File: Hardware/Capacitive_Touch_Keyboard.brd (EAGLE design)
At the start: 170.2 x 68.6 mm, 47 parts, among them J1 AVR_SPI_PRG_6PTH, U2 MC34063DIP, U3 ATMEGA328P_PDIP_EZ, Y1 16MHz

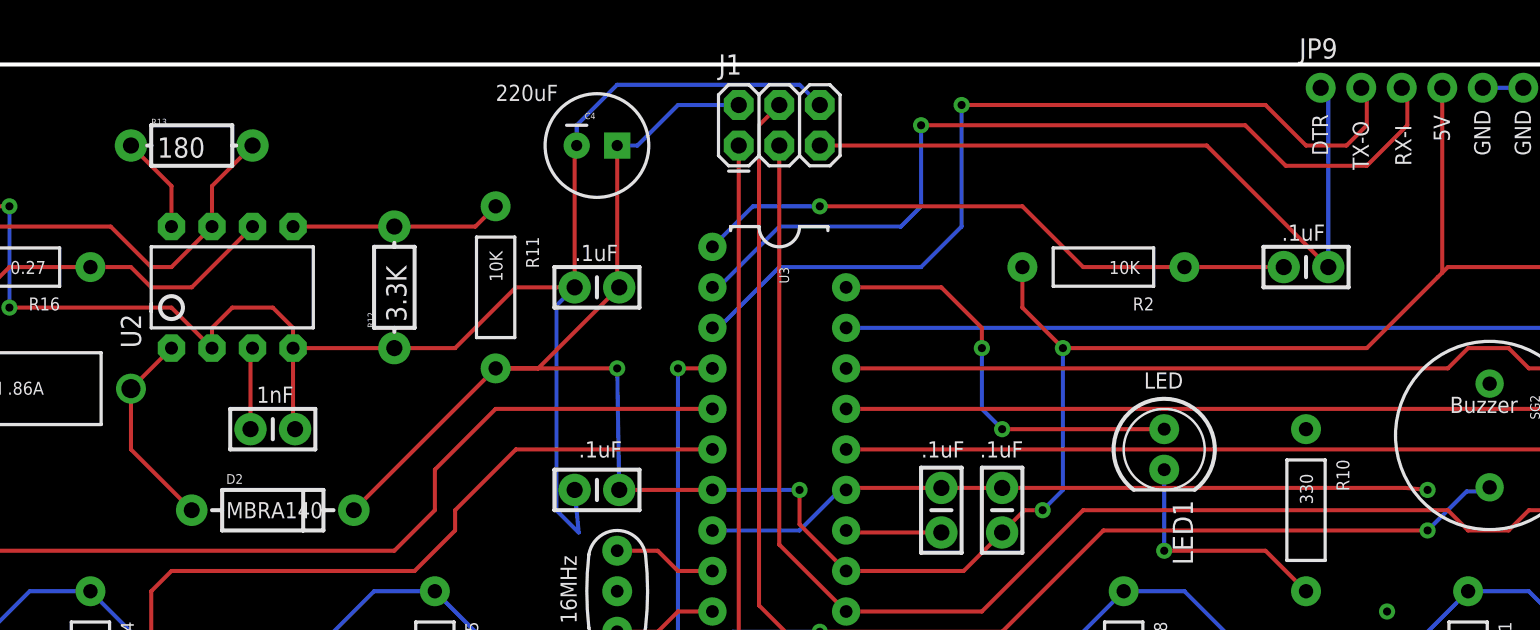
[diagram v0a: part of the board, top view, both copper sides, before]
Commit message: Updated resistor packages for v03
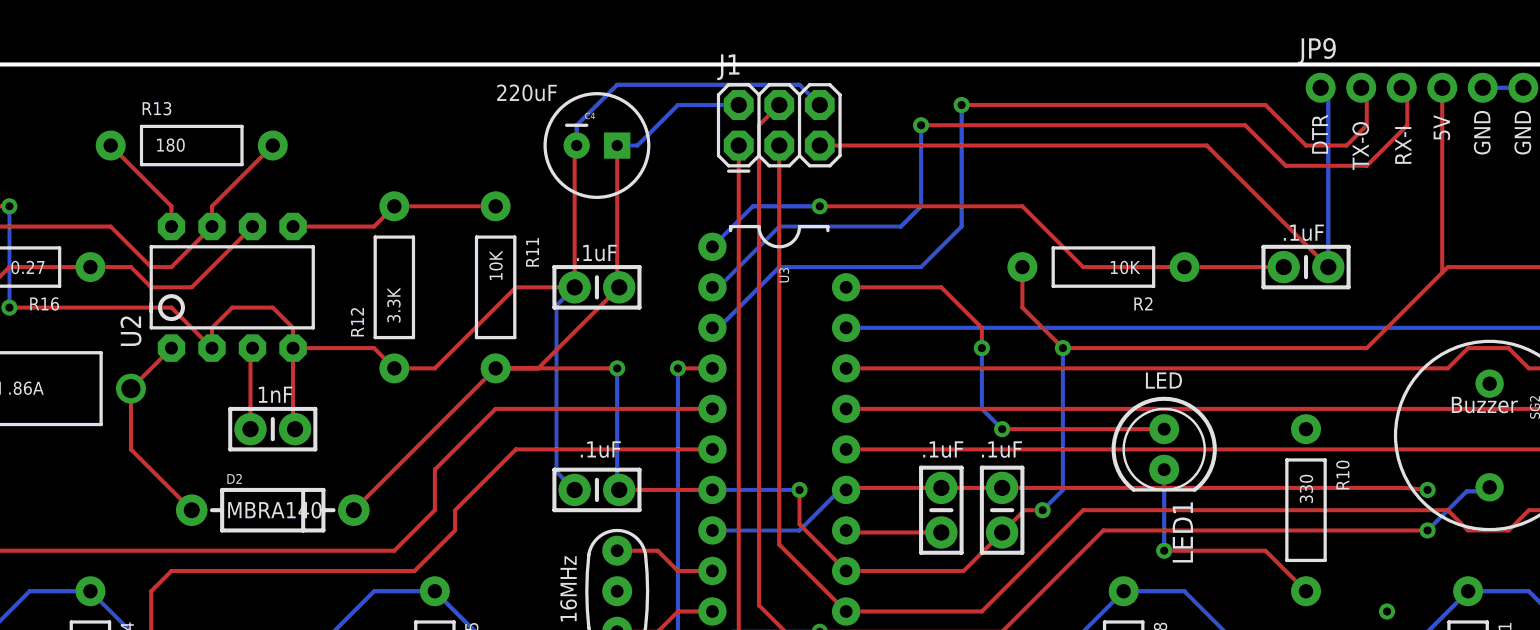
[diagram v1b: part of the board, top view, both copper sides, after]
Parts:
- R12, R13: device SparkFun-Resistors:AXIAL-0.3-KIT -> SparkFun-Resistors:AXIAL-0.4
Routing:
- net GND: track 150.7 -> 146.3 mm
- net N$679: track 6.13 -> 6.66 mm
- net N$678: track 35.7 -> 36.3 mm
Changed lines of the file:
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@@
 <element name="U2" library="SparkFun-PowerIC" package="DIP-08" value="MC34063DIP" x="29.21" y="54.61"/>
 <element name="R11" library="SparkFun-Resistors" package="AXIAL-0.4" value="10K" x="45.72" y="54.61" rot="R270"/>
-<element name="R12" library="SparkFun-Resistors" package="AXIAL-0.3-KIT" value="3.3K" x="39.37" y="54.61" rot="R90"/>
-<element name="R13" library="SparkFun-Resistors" package="AXIAL-0.3-KIT" value="180" x="26.67" y="63.5"/>
+<element name="R12" library="SparkFun-Resistors" package="AXIAL-0.4" value="3.3K" x="39.37" y="54.61" rot="R90"/>
+<element name="R13" library="SparkFun-Resistors" package="AXIAL-0.4" value="180" x="26.67" y="63.5"/>
 <element name="R16" library="SparkFun-Resistors" package="AXIAL-0.4" value="0.27" x="15.24" y="55.88" rot="R180"/>
 <element name="D2" library="SparkFun-DiscreteSemi" package="DIODE-1N4001" value="MBRA140" x="31.75" y="40.64"/>
@@
 <wire x1="33.02" y1="50.8" x2="33.02" y2="45.847" width="0.254" layer="1"/>
 <wire x1="33.02" y1="45.847" x2="33.147" y2="45.72" width="0.254" layer="1"/>
-<wire x1="33.02" y1="50.8" x2="39.37" y2="50.8" width="0.254" layer="1"/>
-<wire x1="39.37" y1="50.8" x2="43.18" y2="50.8" width="0.254" layer="1"/>
-<wire x1="43.18" y1="50.8" x2="46.99" y2="54.61" width="0.254" layer="1"/>
 <wire x1="46.99" y1="54.61" x2="50.673" y2="54.61" width="0.254" layer="1"/>
 <wire x1="50.673" y1="54.61" x2="50.673" y2="63.373" width="0.254" layer="1"/>
 <wire x1="50.673" y1="63.373" x2="50.8" y2="63.5" width="0.254" layer="1"/>
-<wire x1="50.673" y1="41.91" x2="50.927" y2="39.243" width="0.254" layer="16"/>
-<wire x1="50.927" y1="39.243" x2="49.53" y2="40.64" width="0.254" layer="16"/>
-<wire x1="49.53" y1="40.64" x2="49.53" y2="53.467" width="0.254" layer="16"/>
 <wire x1="49.53" y1="53.467" x2="50.673" y2="54.61" width="0.254" layer="16"/>
 <wire x1="77.47" y1="42.037" x2="73.66" y2="42.037" width="0.254" layer="1"/>
@@
 <contactref element="R10" pad="P$1"/>
 <via x="101.6" y="34.29" extent="1-16" drill="0.508"/>
+<wire x1="49.53" y1="53.467" x2="49.53" y2="43.053" width="0.254" layer="16"/>
+<wire x1="49.53" y1="43.053" x2="50.673" y2="41.91" width="0.254" layer="16"/>
+<wire x1="33.02" y1="50.8" x2="38.1" y2="50.8" width="0.254" layer="1"/>
+<wire x1="38.1" y1="50.8" x2="39.37" y2="49.53" width="0.254" layer="1"/>
+<wire x1="39.37" y1="49.53" x2="41.91" y2="49.53" width="0.254" layer="1"/>
+<wire x1="41.91" y1="49.53" x2="46.99" y2="54.61" width="0.254" layer="1"/>
+<wire x1="107.6" y1="48.75" x2="107.6" y2="67.12" width="0" layer="19" extent="16-16"/>
+<wire x1="104.14" y1="41.91" x2="107.6" y2="48.75" width="0" layer="19" extent="16-16"/>
+<wire x1="53.34" y1="35.56" x2="59.182" y2="39.243" width="0" layer="19" extent="1-1"/>
+<wire x1="50.673" y1="41.91" x2="53.34" y2="35.56" width="0" layer="19" extent="1-1"/>
+<wire x1="10.43" y1="62.23" x2="12.97" y2="59.69" width="0" layer="19" extent="1-1"/>
+<wire x1="96.52" y1="45.72" x2="102.743" y2="42.037" width="0" layer="19" extent="1-1"/>
+<wire x1="101.6" y1="34.29" x2="102.743" y2="42.037" width="0" layer="19" extent="1-1"/>
+<wire x1="122.9106" y1="41.3512" x2="108.03" y2="48.574" width="0" layer="19" extent="1-1"/>
+<wire x1="122.9106" y1="34.8488" x2="122.9106" y2="41.3512" width="0" layer="19" extent="1-1"/>
 </signal>
 <signal name="AREF">
@@
 <wire x1="53.34" y1="49.53" x2="45.72" y2="49.53" width="0.254" layer="1"/>
 <wire x1="59.309" y1="41.91" x2="53.467" y2="41.91" width="0.254" layer="1"/>
-<wire x1="53.467" y1="41.91" x2="53.34" y2="49.53" width="0.254" layer="16"/>
 <wire x1="67.691" y1="36.83" x2="75.057" y2="36.83" width="0.254" layer="1"/>
 <wire x1="75.057" y1="36.83" x2="77.47" y2="39.243" width="0.254" layer="1"/>
@@
 <wire x1="78.867" y1="40.64" x2="77.47" y2="39.243" width="0.254" layer="1"/>
 <wire x1="105.06" y1="67.12" x2="105.06" y2="55.53" width="0.254" layer="1"/>
-<wire x1="105.06" y1="55.53" x2="104.775" y2="55.245" width="0.254" layer="1"/>
-<wire x1="104.775" y1="55.245" x2="100.33" y2="50.8" width="0.254" layer="1"/>
+<wire x1="105.06" y1="55.53" x2="100.33" y2="50.8" width="0.254" layer="1"/>
 <wire x1="100.33" y1="50.8" x2="81.28" y2="50.8" width="0.254" layer="1"/>
 <wire x1="59.309" y1="41.91" x2="64.77" y2="41.91" width="0.254" layer="16"/>
@@
 <wire x1="120.65" y1="55.88" x2="105.41" y2="55.88" width="0.254" layer="1"/>
 <wire x1="105.41" y1="55.88" x2="105.06" y2="55.53" width="0.254" layer="1"/>
+<wire x1="53.34" y1="49.53" x2="53.34" y2="42.037" width="0.254" layer="16"/>
+<wire x1="53.34" y1="42.037" x2="53.467" y2="41.91" width="0.254" layer="16"/>
 </signal>
 <signal name="SW_VBATT">
@@
 <wire x1="7.62" y1="48.26" x2="7.62" y2="53.34" width="0.254" layer="16"/>
 <wire x1="7.62" y1="53.34" x2="10.16" y2="55.88" width="0.254" layer="16"/>
-<wire x1="27.94" y1="58.42" x2="27.94" y2="60.96" width="0.254" layer="1"/>
-<wire x1="27.94" y1="60.96" x2="30.48" y2="63.5" width="0.254" layer="1"/>
+<wire x1="27.94" y1="58.42" x2="27.94" y2="59.69" width="0.254" layer="1"/>
+<wire x1="27.94" y1="59.69" x2="31.75" y2="63.5" width="0.254" layer="1"/>
 </signal>
 <signal name="N$679">
 <contactref element="R13" pad="P$1"/>
 <contactref element="U2" pad="8"/>
-<wire x1="25.4" y1="58.42" x2="25.4" y2="60.96" width="0.254" layer="1"/>
-<wire x1="25.4" y1="60.96" x2="22.86" y2="63.5" width="0.254" layer="1"/>
+<wire x1="25.4" y1="58.42" x2="25.4" y2="59.69" width="0.254" layer="1"/>
+<wire x1="25.4" y1="59.69" x2="21.59" y2="63.5" width="0.254" layer="1"/>
 </signal>
 <signal name="N$680">
@@
 <contactref element="R12" pad="P$2"/>
 <contactref element="U2" pad="5"/>
-<wire x1="33.02" y1="58.42" x2="39.37" y2="58.42" width="0.254" layer="1"/>
-<wire x1="39.37" y1="58.42" x2="44.45" y2="58.42" width="0.254" layer="1"/>
-<wire x1="44.45" y1="58.42" x2="45.72" y2="59.69" width="0.254" layer="1"/>
+<wire x1="33.02" y1="58.42" x2="38.1" y2="58.42" width="0.254" layer="1"/>
+<wire x1="38.1" y1="58.42" x2="39.37" y2="59.69" width="0.254" layer="1"/>
+<wire x1="39.37" y1="59.69" x2="45.72" y2="59.69" width="0.254" layer="1"/>
 </signal>
 <signal name="N$681">

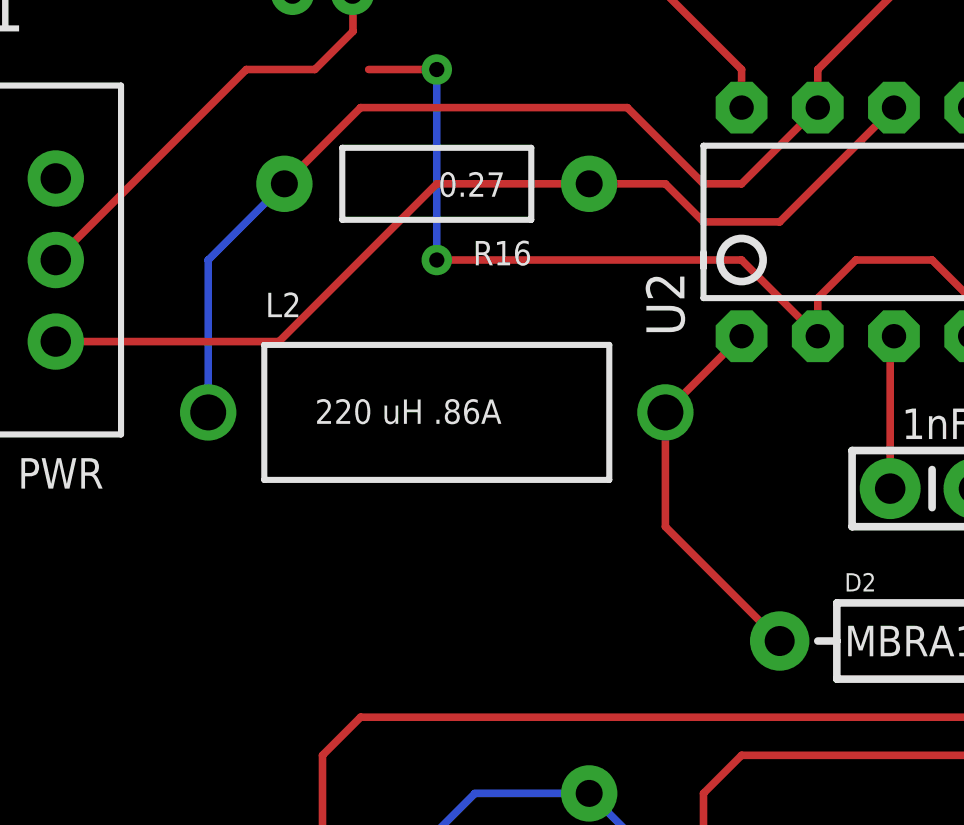
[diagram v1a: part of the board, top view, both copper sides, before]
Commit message: Updated inductor package for v03
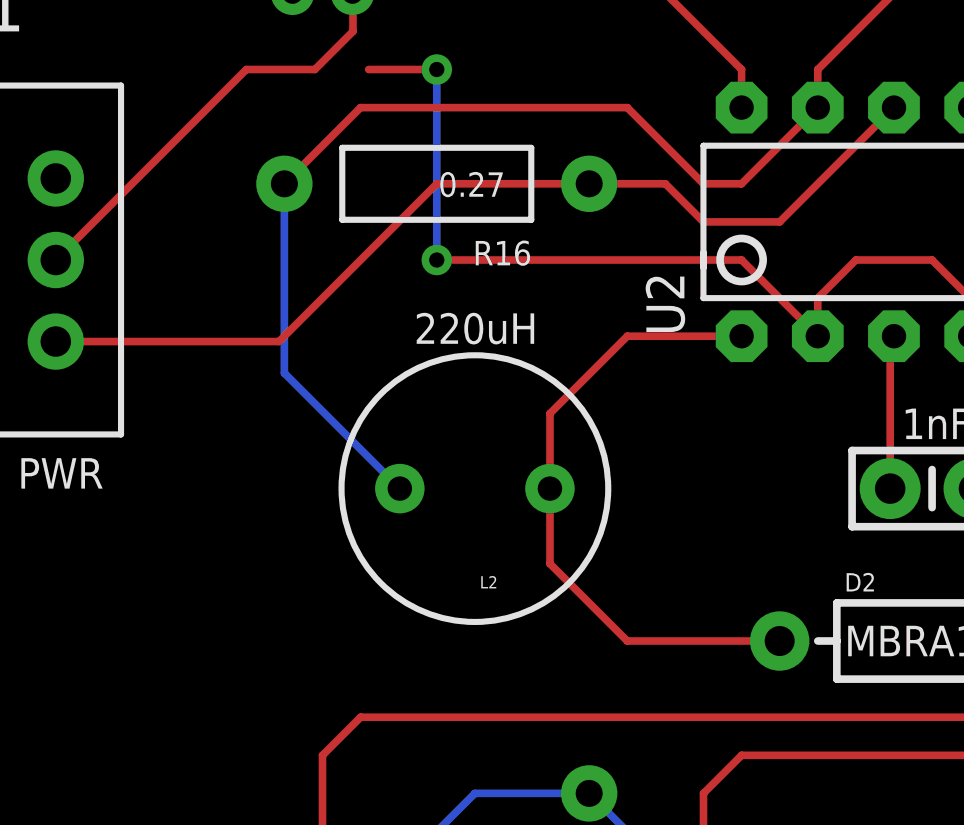
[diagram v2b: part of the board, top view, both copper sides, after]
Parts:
- L2: value 220 uH .86A -> 220 uH .44A; device SparkFun-Passives:AXIAL-0.6 -> SparkFun-Passives:RLB0912
- moved L2 2.84 mm to (16.5, 45.7), turned to 180 degrees
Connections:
- net N$677: now also L2.2; no longer L2.P$2
- net N$678: now also L2.1; no longer L2.P$1
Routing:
- net N$677: track 12.8 -> 21.2 mm
- net N$678: track 36.3 -> 39.3 mm
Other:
- board text added: "220uH"
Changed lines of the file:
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@@
 <text x="105.537" y="46.736" size="1.016" layer="21" font="vector" ratio="15">Buzzer</text>
 <text x="1.27" y="45.72" size="1.016" layer="21" font="vector" ratio="15">PWR</text>
+<text x="14.478" y="50.546" size="1.016" layer="21" font="vector" ratio="15">220uH</text>
 </plain>
 <attributes>
@@
 <element name="C19" library="SparkFun-Capacitors" package="CAP-PTH-SMALL-KIT" value="0.1uF" x="52.07" y="54.61" rot="R180"/>
 <element name="C4" library="SparkFun-Capacitors" package="CPOL-RADIAL-100UF-25V" value="220uF" x="52.07" y="63.5"/>
-<element name="L2" library="SparkFun-Passives" package="AXIAL-0.6" value="220 uH .86A" x="15.24" y="48.26"/>
+<element name="L2" library="SparkFun-Passives" package="RLB0912" value="220 uH .44A" x="16.51" y="45.72" rot="R180"/>
 <element name="U3" library="SparkFun-DigitalIC" package="DIL28-EZ" value="ATMEGA328P_PDIP_EZ" x="63.5" y="40.64" rot="R270"/>
 <element name="R17" library="SparkFun-Resistors" package="AXIAL-0.4" value="1M" x="52.07" y="22.86" rot="R270"/>
@@
 <wire x1="39.37" y1="49.53" x2="41.91" y2="49.53" width="0.254" layer="1"/>
 <wire x1="41.91" y1="49.53" x2="46.99" y2="54.61" width="0.254" layer="1"/>
-<wire x1="107.6" y1="48.75" x2="107.6" y2="67.12" width="0" layer="19" extent="16-16"/>
-<wire x1="104.14" y1="41.91" x2="107.6" y2="48.75" width="0" layer="19" extent="16-16"/>
-<wire x1="53.34" y1="35.56" x2="59.182" y2="39.243" width="0" layer="19" extent="1-1"/>
-<wire x1="50.673" y1="41.91" x2="53.34" y2="35.56" width="0" layer="19" extent="1-1"/>
-<wire x1="10.43" y1="62.23" x2="12.97" y2="59.69" width="0" layer="19" extent="1-1"/>
-<wire x1="96.52" y1="45.72" x2="102.743" y2="42.037" width="0" layer="19" extent="1-1"/>
-<wire x1="101.6" y1="34.29" x2="102.743" y2="42.037" width="0" layer="19" extent="1-1"/>
-<wire x1="122.9106" y1="41.3512" x2="108.03" y2="48.574" width="0" layer="19" extent="1-1"/>
-<wire x1="122.9106" y1="34.8488" x2="122.9106" y2="41.3512" width="0" layer="19" extent="1-1"/>
 </signal>
 <signal name="AREF">
@@
 <contactref element="D2" pad="A"/>
 <contactref element="U2" pad="1"/>
-<contactref element="L2" pad="P$2"/>
-<wire x1="22.86" y1="48.26" x2="25.4" y2="50.8" width="0.254" layer="1"/>
-<wire x1="22.86" y1="48.26" x2="22.86" y2="44.45" width="0.254" layer="1"/>
-<wire x1="22.86" y1="44.45" x2="26.67" y2="40.64" width="0.254" layer="1"/>
+<contactref element="L2" pad="2"/>
+<wire x1="19.0119" y1="45.72" x2="19.0119" y2="43.2181" width="0.254" layer="1"/>
+<wire x1="19.0119" y1="43.2181" x2="21.59" y2="40.64" width="0.254" layer="1"/>
+<wire x1="21.59" y1="40.64" x2="26.67" y2="40.64" width="0.254" layer="1"/>
+<wire x1="19.0119" y1="45.72" x2="19.0119" y2="48.2219" width="0.254" layer="1"/>
+<wire x1="19.0119" y1="48.2219" x2="21.59" y2="50.8" width="0.254" layer="1"/>
+<wire x1="21.59" y1="50.8" x2="25.4" y2="50.8" width="0.254" layer="1"/>
 </signal>
 <signal name="N$678">
@@
 <contactref element="R16" pad="P$2"/>
 <contactref element="U2" pad="7"/>
-<contactref element="L2" pad="P$1"/>
+<contactref element="L2" pad="1"/>
 <wire x1="27.94" y1="58.42" x2="25.4" y2="55.88" width="0.254" layer="1"/>
 <wire x1="25.4" y1="55.88" x2="24.13" y2="55.88" width="0.254" layer="1"/>
@@
 <wire x1="21.59" y1="58.42" x2="12.7" y2="58.42" width="0.254" layer="1"/>
 <wire x1="12.7" y1="58.42" x2="10.16" y2="55.88" width="0.254" layer="1"/>
-<wire x1="7.62" y1="48.26" x2="7.62" y2="53.34" width="0.254" layer="16"/>
-<wire x1="7.62" y1="53.34" x2="10.16" y2="55.88" width="0.254" layer="16"/>
 <wire x1="27.94" y1="58.42" x2="27.94" y2="59.69" width="0.254" layer="1"/>
 <wire x1="27.94" y1="59.69" x2="31.75" y2="63.5" width="0.254" layer="1"/>
+<wire x1="10.16" y1="55.88" x2="10.16" y2="49.5681" width="0.254" layer="16"/>
+<wire x1="10.16" y1="49.5681" x2="14.0081" y2="45.72" width="0.254" layer="16"/>
 </signal>
 <signal name="N$679">

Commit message: v04 protos, ready for review
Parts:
- removed C17: 1000pF, SparkFun-Capacitors:CAP-PTH-SMALL-KIT
- removed C19: 0.1uF, SparkFun-Capacitors:CAP-PTH-SMALL-KIT
- removed C4: 220uF, SparkFun-Capacitors:CPOL-RADIAL-100UF-25V
- removed D2: MBRA140, SparkFun-DiscreteSemi:DIODE-1N4001
- removed JP1: (no value), SparkFun-Connectors:JST-2-PTH-KIT
- removed L2: 220 uH .44A, SparkFun-Passives:RLB0912
- removed R13: 180, SparkFun-Resistors:AXIAL-0.4
- removed R16: 0.27, SparkFun-Resistors:AXIAL-0.4
- removed SG2: BUZZER, SparkFun-Electromechanical:BUZZER-12MM
- removed U2: MC34063DIP, SparkFun-PowerIC:DIP-08
- removed Y1: 16MHz, SparkFun-FreqCtrl:RESONATOR-PTH
- added BAT1, BAT2: (no value), SparkFun-Electromechanical:BATTERY-AA-KIT
- added LED2: Red, SparkFun-LED:LED5MM-KIT
- added SP1: SPEAKERPCB_MOUNT, SparkFun-Electromechanical:PCB_MOUNT_SPEAKER
- R11: value 10K -> TRIMPOT-PTH-KNOB; device SparkFun-Resistors:AXIAL-0.4 -> SparkFun-Electromechanical:3386U
- R12: value 3.3K -> 330
- moved S1 163.8 mm to (166.4, 53.3)
- moved R12 124.9 mm to (162.6, 34.3), turned to 0 degrees
- moved S2 114.9 mm to (6.35, 49.5)
- moved R14 111.9 mm to (8.89, 57.1), turned to 0 degrees
- moved R11 43.2 mm to (6.35, 36.8), turned to 0 degrees
- moved STANDOFF2 24.2 mm to (167.6, 2.54)
- moved STANDOFF3 24.2 mm to (2.54, 2.54)
- moved LOGO1 21.9 mm to (132.7, 30.2)
- moved JP9 15.2 mm to (82.2, 67.1)
- moved C2 5.08 mm to (91.4, 55.9)
- moved R2 2.54 mm to (81.3, 55.9)
- moved LOGO2 2.05 mm to (93.0, 46.5)
- moved LOGO3 1.80 mm to (163.8, 6.35)
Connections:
- removed net 5V: C10.1, C19.1, C3.2, C4.1, D2.C, J1.2, JP9.4, R11.P$2, R14.P$2, R2.P$2, U3.20, U3.7
- removed net BUZZER: SG2.+, U3.11
- removed net N$2: U3.9, Y1.1
- removed net N$677: D2.A, L2.2, U2.1
- removed net N$678: L2.1, R13.P$2, R16.P$2, U2.7
- removed net N$679: R13.P$1, U2.8
- removed net N$680: R11.P$1, R12.P$2, U2.5
- removed net N$681: C17.1, U2.3
- removed net RAW_IN: R16.P$1, S1.3, U2.6
- removed net SW_VBATT: JP1.2, S1.2
- new net 3.3V: C10.1, C3.2, J1.2, JP9.4, LED2.A, R11.3, R14.P$2, R2.P$2, S1.3, U3.20, U3.7
- new net BUTTON: R14.P$1, S2.1, S2.2, U3.9
- new net N$3: BAT1.GND@1, BAT2.PWR@1
- new net SPEAKER: SP1.+, U3.11
- new net VBATT: BAT1.PWR@1, S1.2
- net A3: now also R11.2; no longer R14.P$1, S2.1, S2.2
- net DTR: no longer J1.5
- net GND: now also BAT2.GND@1, R11.1, SP1.-; no longer C17.2, C19.2, C4.2, JP1.1, SG2.-, U2.2, U2.4, Y1.2
- net N$1: now also LED2.K, R12.P$2; no longer U3.10, Y1.3
- net RESET: now also J1.5
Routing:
- net 3.3V: track 0.00 -> 253.9 mm, vias 0 -> 5
- net 5V: track 156.7 -> 0.00 mm, vias 4 -> 0
- net GND: track 146.3 -> 257.5 mm, vias 4 -> 7
- net BUTTON: track 0.00 -> 70.4 mm, vias 0 -> 2
- net BUZZER: track 53.0 -> 0.00 mm, vias 2 -> 0
- net N$678: track 39.3 -> 0.00 mm
- net SPEAKER: track 0.00 -> 33.6 mm, vias 0 -> 2
- net RAW_IN: track 32.2 -> 0.00 mm
- net DTR: track 46.5 -> 20.3 mm, vias 0 -> 1
- net N$677: track 21.2 -> 0.00 mm
- net TX-O: track 55.3 -> 35.4 mm
- net RX-I: track 55.3 -> 35.4 mm
- net N$3: track 0.00 -> 15.2 mm
- net SW_VBATT: track 14.3 -> 0.00 mm
- net N$680: track 13.2 -> 0.00 mm
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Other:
- board text added: "+"
- board text added: "-"
- board text added: "3.3V"
- board text added: "OFF"
- board text added: "ON"
- board text added: "Speaker"
- board text added: "v04"
- board text removed: "16MHz"
- board text removed: "1nF"
- board text removed: "220uF"
- board text removed: "220uH"
- board text removed: "5V"
- board text removed: "Buzzer"
- board text removed: "v03"

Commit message: v04, made changes from design review
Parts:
- moved JP9 12.6 mm to (94.8, 67.1), turned to 180 degrees
- moved C3 1.89 mm to (53.3, 40.5), turned to 90 degrees
- moved STANDOFF4 1.80 mm to (2.54, 66.0)
- moved STANDOFF1 1.80 mm to (167.6, 66.0)
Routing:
- net GND: track 257.5 -> 265.9 mm
- net DTR: track 20.3 -> 12.1 mm, vias 1 -> 0
- net TX-O: track 35.4 -> 40.7 mm
- net 3.3V: track 253.9 -> 255.9 mm, vias 5 -> 6
- net RX-I: track 35.4 -> 37.1 mm
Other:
- board text added: "A"
- board text added: "B"
- board text added: "BLK"
- board text added: "C"
- board text added: "D"
- board text added: "E"
- board text added: "F"
- board text added: "G"
- board text added: "GRN"
